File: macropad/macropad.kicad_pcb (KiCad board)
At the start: 2 copper layers, 19.9 x 58.5 mm, 4 parts, among them SW1 SW_Push, SW2 SW_Push, SW3 SW_Push, U1 MOUDLE-SEEEDUINO-XIAO

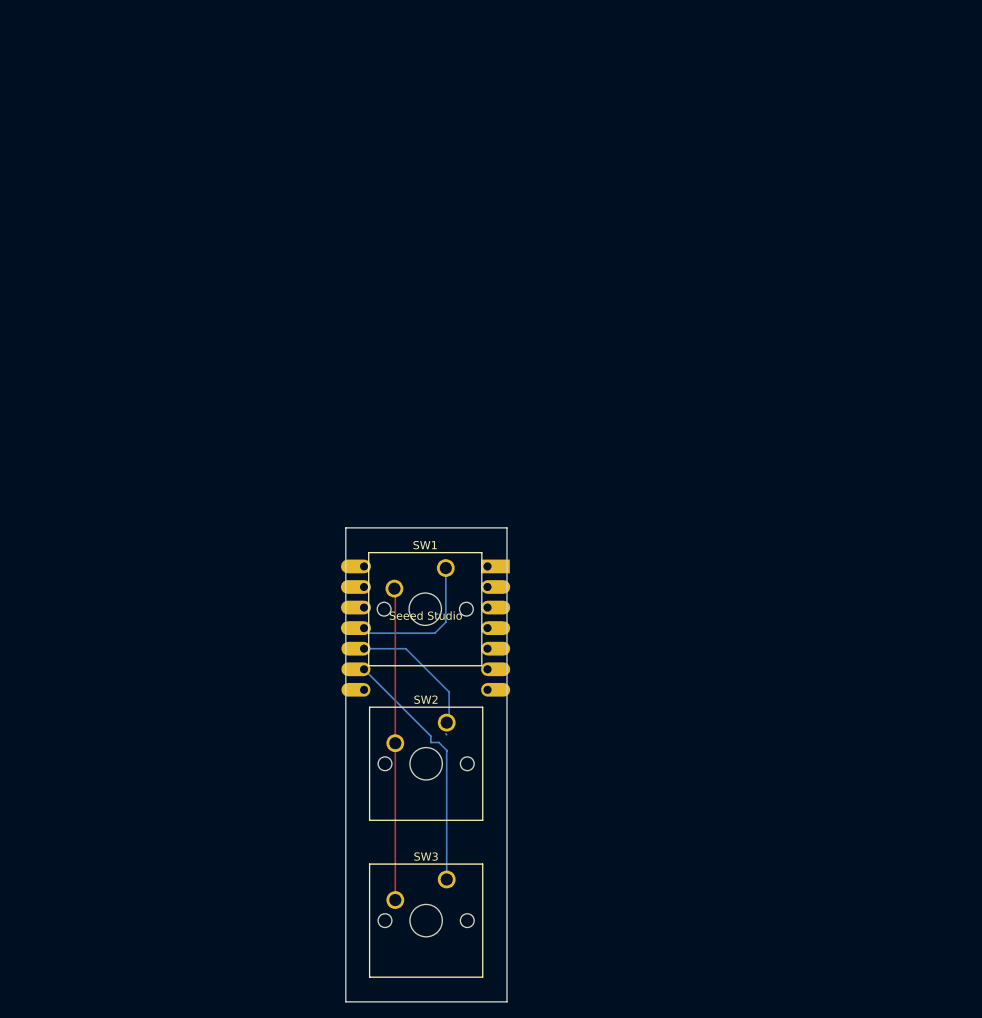
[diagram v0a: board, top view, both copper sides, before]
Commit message: Footprint edits
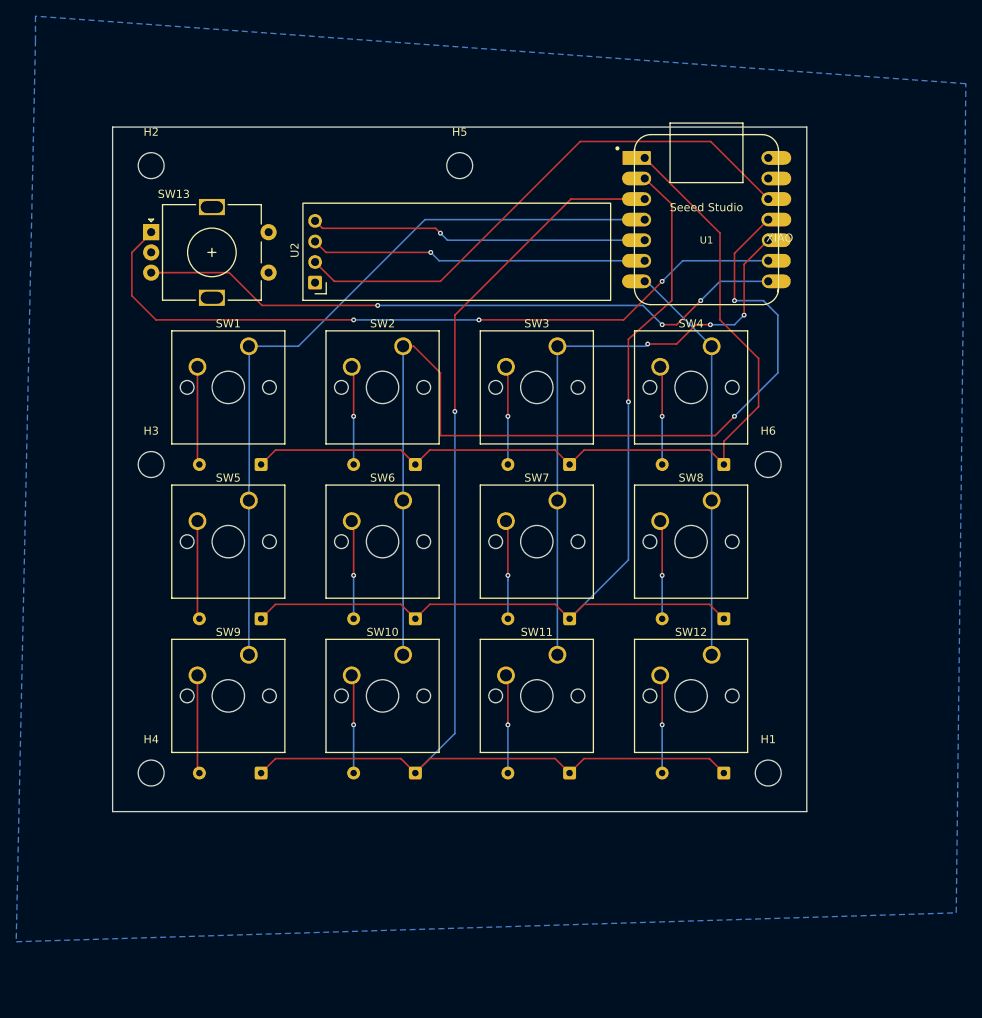
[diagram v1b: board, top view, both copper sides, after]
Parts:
- added D1: 1N4148, Diode_THT:D_DO-35_SOD27_P7.62mm_Horizontal, B.Cu at (94.5, 66.7)
- added D10: 1N4148, Diode_THT:D_DO-35_SOD27_P7.62mm_Horizontal, B.Cu at (113.6, 104.8)
- added D11: 1N4148, Diode_THT:D_DO-35_SOD27_P7.62mm_Horizontal, B.Cu at (132.6, 104.8)
- added D12: 1N4148, Diode_THT:D_DO-35_SOD27_P7.62mm_Horizontal, B.Cu at (151.7, 104.8)
- added D2: 1N4148, Diode_THT:D_DO-35_SOD27_P7.62mm_Horizontal, B.Cu at (113.6, 66.7)
- added D3: 1N4148, Diode_THT:D_DO-35_SOD27_P7.62mm_Horizontal, B.Cu at (132.6, 66.7)
- added D4: 1N4148, Diode_THT:D_DO-35_SOD27_P7.62mm_Horizontal, B.Cu at (151.7, 66.7)
- added D5: 1N4148, Diode_THT:D_DO-35_SOD27_P7.62mm_Horizontal, B.Cu at (94.5, 85.7)
- added D6: 1N4148, Diode_THT:D_DO-35_SOD27_P7.62mm_Horizontal, B.Cu at (113.6, 85.7)
- added D7: 1N4148, Diode_THT:D_DO-35_SOD27_P7.62mm_Horizontal, B.Cu at (132.6, 85.7)
- added D8: 1N4148, Diode_THT:D_DO-35_SOD27_P7.62mm_Horizontal, B.Cu at (151.7, 85.7)
- added D9: 1N4148, Diode_THT:D_DO-35_SOD27_P7.62mm_Horizontal, B.Cu at (94.5, 104.8)
- added H1: MountingHole, MountingHole:MountingHole_3.2mm_M3, F.Cu at (157.2, 104.8)
- added H2: MountingHole, MountingHole:MountingHole_3.2mm_M3, F.Cu at (81.0, 29.8)
- added H3: MountingHole, MountingHole:MountingHole_3.2mm_M3, F.Cu at (81.0, 66.7)
- added H4: MountingHole, MountingHole:MountingHole_3.2mm_M3, F.Cu at (81.0, 104.8)
- added H5: MountingHole, MountingHole:MountingHole_3.2mm_M3, F.Cu at (119.1, 29.8)
- added H6: MountingHole, MountingHole:MountingHole_3.2mm_M3, F.Cu at (157.2, 66.7)
- added SW10: SW_Push, Button_Switch_Keyboard:SW_Cherry_MX_1.00u_PCB, F.Cu at (112.1, 90.2)
- added SW11: SW_Push, Button_Switch_Keyboard:SW_Cherry_MX_1.00u_PCB, F.Cu at (131.1, 90.2)
- added SW12: SW_Push, Button_Switch_Keyboard:SW_Cherry_MX_1.00u_PCB, F.Cu at (150.2, 90.2)
- added SW13: RotaryEncoder_Switch, Rotary_Encoder:RotaryEncoder_Alps_EC11E-Switch_Vertical_H20mm, F.Cu at (81.0, 38.0)
- added SW4: SW_Push, Button_Switch_Keyboard:SW_Cherry_MX_1.00u_PCB, F.Cu at (150.2, 52.1)
- added SW5: SW_Push, Button_Switch_Keyboard:SW_Cherry_MX_1.00u_PCB, F.Cu at (93.0, 71.1)
- added SW6: SW_Push, Button_Switch_Keyboard:SW_Cherry_MX_1.00u_PCB, F.Cu at (112.1, 71.1)
- added SW7: SW_Push, Button_Switch_Keyboard:SW_Cherry_MX_1.00u_PCB, F.Cu at (131.1, 71.1)
- added SW8: SW_Push, Button_Switch_Keyboard:SW_Cherry_MX_1.00u_PCB, F.Cu at (150.2, 71.1)
- added SW9: SW_Push, Button_Switch_Keyboard:SW_Cherry_MX_1.00u_PCB, F.Cu at (93.0, 90.2)
- added U2: ER_OLEDM0.91_1x-I2C, Display:ER_OLEDM0.91_1x-I2C, F.Cu at (101.2, 44.2)
- U1: moved to F.Cu
- moved SW3 67.3 mm to (131.1, 52.1)
- moved U1 61.2 mm to (149.5, 36.4), turned to 0 degrees
- moved SW2 46.8 mm to (112.1, 52.1)
- moved SW1 36.6 mm to (93.0, 52.1)
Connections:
- SW1 pad 1: Net-(U1-PA6_A10_D10_MOSI) -> Col 0
- SW1 pad 2: GND -> Net-(D1-A)
- SW2 pad 1: Net-(U1-PA5_A9_D9_MISO) -> Col 1
- SW2 pad 2: GND -> Net-(D2-A)
- SW3 pad 1: Net-(U1-PA7_A8_D8_SCK) -> Col 2
- SW3 pad 2: GND -> Net-(D3-A)
- U1 pad 1: unconnected-(U1-PA02_A0_D0-Pad1) -> Row 0
- U1 pad 10: Net-(U1-PA5_A9_D9_MISO) -> Col 2
- U1 pad 11: Net-(U1-PA6_A10_D10_MOSI) -> Col 1
- U1 pad 12: unconnected-(U1-3V3-Pad12) -> VCC
- U1 pad 2: unconnected-(U1-PA4_A1_D1-Pad2) -> Row 1
- U1 pad 3: unconnected-(U1-PA10_A2_D2-Pad3) -> Row 2
- U1 pad 4: unconnected-(U1-PA11_A3_D3-Pad4) -> Col 0
- U1 pad 5: unconnected-(U1-PA8_A4_D4_SDA-Pad5) -> Net-(U1-PA8_A4_D4_SDA)
- U1 pad 6: unconnected-(U1-PA9_A5_D5_SCL-Pad6) -> Net-(U1-PA9_A5_D5_SCL)
- U1 pad 7: unconnected-(U1-PB08_A6_D6_TX-Pad7) -> Col 3
- U1 pad 8: unconnected-(U1-PB09_A7_D7_RX-Pad8) -> Net-(U1-PB09_A7_D7_RX)
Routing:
- net Row 2: track 0.00 -> 149.5 mm, vias 0 -> 1
- net Row 1: track 0.00 -> 122.8 mm, vias 0 -> 1
- net Col 1: track 0.00 -> 121.7 mm, vias 0 -> 2
- net Row 0: track 0.00 -> 107.1 mm
- net Col 0: track 0.00 -> 94.1 mm
- net Net-(U1-PB09_A7_D7_RX): track 0.00 -> 81.1 mm, vias 0 -> 3
- net Col 2: track 0.00 -> 73.2 mm, vias 0 -> 3
- net VCC: track 0.00 -> 67.0 mm
- net Net-(U1-PA7_A8_D8_SCK): track 31.0 -> 91.7 mm, vias 0 -> 3
- net Col 3: track 0.00 -> 49.7 mm
- net Net-(U1-PA9_A5_D5_SCL): track 0.00 -> 41.7 mm, vias 0 -> 1
- net Net-(U1-PA8_A4_D4_SDA): track 0.00 -> 41.7 mm, vias 0 -> 1
- net GND: track 37.8 -> 0.00 mm
- net Net-(U1-PA6_A10_D10_MOSI): track 17.6 -> 0.00 mm
- net Net-(U1-PA5_A9_D9_MISO): track 16.5 -> 0.00 mm
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- added copper zone on B.Cu, net GND
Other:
- board size 19.9 x 58.5 mm -> 85.7 x 84.5 mm

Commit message: Add rotary encoder step file
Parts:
- SW1, SW10, SW11, SW12, SW2, SW3, SW4, SW5, SW6, SW7, SW8, SW9: footprint Button_Switch_Keyboard:SW_Cherry_MX_1.00u_PCB -> footprints:SW_Cherry_MX_1.00u_PCB_(3D_STEP)
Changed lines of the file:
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@@
 		(embedded_fonts no)
 	)
-	(footprint "Button_Switch_Keyboard:SW_Cherry_MX_1.00u_PCB"
+	(footprint "footprints:SW_Cherry_MX_1.00u_PCB_(3D_STEP)"
 		(layer "F.Cu")
 		(at 112.0775 71.12)
@@
 		(embedded_fonts no)
 		(model "${KICAD10_3DMODEL_DIR}/Button_Switch_Keyboard.3dshapes/SW_Cherry_MX_1.00u_PCB.step"
+			(hide yes)
 			(offset
 				(xyz 0 0 0)
@@
 			)
 		)
+		(model "${KIPRJMOD}/kicad_care_package/MX .STEP"
+			(offset
+				(xyz 4.75 2.25 5.75)
+			)
+			(scale
+				(xyz 1 1 1)
+			)
+			(rotate
+				(xyz -90 -0 -180)
+			)
+		)
 	)
-	(footprint "Button_Switch_Keyboard:SW_Cherry_MX_1.00u_PCB"
+	(footprint "footprints:SW_Cherry_MX_1.00u_PCB_(3D_STEP)"
 		(layer "F.Cu")
 		(at 112.0775 52.07)
@@
 		(embedded_fonts no)
 		(model "${KICAD10_3DMODEL_DIR}/Button_Switch_Keyboard.3dshapes/SW_Cherry_MX_1.00u_PCB.step"
+			(hide yes)
 			(offset
 				(xyz 0 0 0)
@@
 			)
 		)
+		(model "${KIPRJMOD}/kicad_care_package/MX .STEP"
+			(offset
+				(xyz 4.75 2.25 5.75)
+			)
+			(scale
+				(xyz 1 1 1)
+			)
+			(rotate
+				(xyz -90 -0 -180)
+			)
+		)
 	)
 	(footprint "MountingHole:MountingHole_3.2mm_M3"
@@
 		(embedded_fonts no)
 	)
-	(footprint "Button_Switch_Keyboard:SW_Cherry_MX_1.00u_PCB"
+	(footprint "footprints:SW_Cherry_MX_1.00u_PCB_(3D_STEP)"
 		(layer "F.Cu")
 		(at 150.1775 90.17)
@@
 		(embedded_fonts no)
 		(model "${KICAD10_3DMODEL_DIR}/Button_Switch_Keyboard.3dshapes/SW_Cherry_MX_1.00u_PCB.step"
+			(hide yes)
 			(offset
 				(xyz 0 0 0)
@@
 			)
 		)
+		(model "${KIPRJMOD}/kicad_care_package/MX .STEP"
+			(offset
+				(xyz 4.75 2.25 5.75)
+			)
+			(scale
+				(xyz 1 1 1)
+			)
+			(rotate
+				(xyz -90 -0 -180)
+			)
+		)
 	)
-	(footprint "Button_Switch_Keyboard:SW_Cherry_MX_1.00u_PCB"
+	(footprint "footprints:SW_Cherry_MX_1.00u_PCB_(3D_STEP)"
 		(layer "F.Cu")
 		(at 93.0275 52.07)
@@
 		(embedded_fonts no)
 		(model "${KICAD10_3DMODEL_DIR}/Button_Switch_Keyboard.3dshapes/SW_Cherry_MX_1.00u_PCB.step"
+			(hide yes)
 			(offset
 				(xyz 0 0 0)
@@
 			)
 		)
+		(model "${KIPRJMOD}/kicad_care_package/MX .STEP"
+			(offset
+				(xyz 4.75 2.25 5.75)
+			)
+			(scale
+				(xyz 1 1 1)
+			)
+			(rotate
+				(xyz -90 -0 -180)
+			)
+		)
 	)
-	(footprint "Button_Switch_Keyboard:SW_Cherry_MX_1.00u_PCB"
+	(footprint "footprints:SW_Cherry_MX_1.00u_PCB_(3D_STEP)"
 		(layer "F.Cu")
 		(at 93.0275 90.17)
@@
 		(embedded_fonts no)
 		(model "${KICAD10_3DMODEL_DIR}/Button_Switch_Keyboard.3dshapes/SW_Cherry_MX_1.00u_PCB.step"
+			(hide yes)
 			(offset
 				(xyz 0 0 0)
@@
 			)
 		)
+		(model "${KIPRJMOD}/kicad_care_package/MX .STEP"
+			(offset
+				(xyz 4.75 2.25 5.75)
+			)
+			(scale
+				(xyz 1 1 1)
+			)
+			(rotate
+				(xyz -90 -0 -180)
+			)
+		)
 	)
 	(footprint "MountingHole:MountingHole_3.2mm_M3"
@@
 		(embedded_fonts no)
 	)
-	(footprint "Button_Switch_Keyboard:SW_Cherry_MX_1.00u_PCB"
+	(footprint "footprints:SW_Cherry_MX_1.00u_PCB_(3D_STEP)"
 		(layer "F.Cu")
 		(at 112.0775 90.17)
@@
 		(embedded_fonts no)
 		(model "${KICAD10_3DMODEL_DIR}/Button_Switch_Keyboard.3dshapes/SW_Cherry_MX_1.00u_PCB.step"
+			(hide yes)
 			(offset
 				(xyz 0 0 0)
@@
 			)
 		)
+		(model "${KIPRJMOD}/kicad_care_package/MX .STEP"
+			(offset
+				(xyz 4.75 2.25 5.75)
+			)
+			(scale
+				(xyz 1 1 1)
+			)
+			(rotate
+				(xyz -90 -0 -180)
+			)
+		)
 	)
-	(footprint "Button_Switch_Keyboard:SW_Cherry_MX_1.00u_PCB"
+	(footprint "footprints:SW_Cherry_MX_1.00u_PCB_(3D_STEP)"
 		(layer "F.Cu")
 		(at 93.0275 71.12)
@@
 		(embedded_fonts no)
 		(model "${KICAD10_3DMODEL_DIR}/Button_Switch_Keyboard.3dshapes/SW_Cherry_MX_1.00u_PCB.step"
+			(hide yes)
 			(offset
 				(xyz 0 0 0)
@@
 			)
 		)
+		(model "${KIPRJMOD}/kicad_care_package/MX .STEP"
+			(offset
+				(xyz 4.75 2.25 5.75)
+			)
+			(scale
+				(xyz 1 1 1)
+			)
+			(rotate
+				(xyz -90 -0 -180)
+			)
+		)
 	)
 	(footprint "MountingHole:MountingHole_3.2mm_M3"
@@
 		)
 	)
-	(footprint "Button_Switch_Keyboard:SW_Cherry_MX_1.00u_PCB"
+	(footprint "footprints:SW_Cherry_MX_1.00u_PCB_(3D_STEP)"
 		(layer "F.Cu")
 		(at 150.1775 71.12)
@@
 		(embedded_fonts no)
 		(model "${KICAD10_3DMODEL_DIR}/Button_Switch_Keyboard.3dshapes/SW_Cherry_MX_1.00u_PCB.step"
+			(hide yes)
 			(offset
 				(xyz 0 0 0)
@@
 			)
 		)
+		(model "${KIPRJMOD}/kicad_care_package/MX .STEP"
+			(offset
+				(xyz 4.75 2.25 5.75)
+			)
+			(scale
+				(xyz 1 1 1)
+			)
+			(rotate
+				(xyz -90 -0 -180)
+			)
+		)
 	)
 	(footprint "MountingHole:MountingHole_3.2mm_M3"
@@
 		)
 	)
-	(footprint "Button_Switch_Keyboard:SW_Cherry_MX_1.00u_PCB"
+	(footprint "footprints:SW_Cherry_MX_1.00u_PCB_(3D_STEP)"
 		(layer "F.Cu")
 		(at 131.1275 90.17)
@@
 		(embedded_fonts no)
 		(model "${KICAD10_3DMODEL_DIR}/Button_Switch_Keyboard.3dshapes/SW_Cherry_MX_1.00u_PCB.step"
+			(hide yes)
 			(offset
 				(xyz 0 0 0)
@@
 			)
 		)
+		(model "${KIPRJMOD}/kicad_care_package/MX .STEP"
+			(offset
+				(xyz 4.75 2.25 5.75)
+			)
+			(scale
+				(xyz 1 1 1)
+			)
+			(rotate
+				(xyz -90 -0 -180)
+			)
+		)
 	)
-	(footprint "Button_Switch_Keyboard:SW_Cherry_MX_1.00u_PCB"
+	(footprint "footprints:SW_Cherry_MX_1.00u_PCB_(3D_STEP)"
 		(layer "F.Cu")
 		(at 131.1275 52.07)
@@
 		(embedded_fonts no)
 		(model "${KICAD10_3DMODEL_DIR}/Button_Switch_Keyboard.3dshapes/SW_Cherry_MX_1.00u_PCB.step"
+			(hide yes)
 			(offset
 				(xyz 0 0 0)
@@
 			)
 		)
+		(model "${KIPRJMOD}/kicad_care_package/MX .STEP"
+			(offset
+				(xyz 4.75 2.25 5.75)
+			)
+			(scale
+				(xyz 1 1 1)
+			)
+			(rotate
+				(xyz -90 -0 -180)
+			)
+		)
 	)
 	(footprint "MountingHole:MountingHole_3.2mm_M3"
@@
 		(embedded_fonts no)
 	)
-	(footprint "Button_Switch_Keyboard:SW_Cherry_MX_1.00u_PCB"
+	(footprint "footprints:SW_Cherry_MX_1.00u_PCB_(3D_STEP)"
 		(layer "F.Cu")
 		(at 150.1775 52.07)
@@
 		(embedded_fonts no)
 		(model "${KICAD10_3DMODEL_DIR}/Button_Switch_Keyboard.3dshapes/SW_Cherry_MX_1.00u_PCB.step"
+			(hide yes)
 			(offset
 				(xyz 0 0 0)
@@
 			)
 		)
+		(model "${KIPRJMOD}/kicad_care_package/MX .STEP"
+			(offset
+				(xyz 4.75 2.25 5.75)
+			)
+			(scale
+				(xyz 1 1 1)
+			)
+			(rotate
+				(xyz -90 -0 -180)
+			)
+		)
 	)
-	(footprint "Button_Switch_Keyboard:SW_Cherry_MX_1.00u_PCB"
+	(footprint "footprints:SW_Cherry_MX_1.00u_PCB_(3D_STEP)"
 		(layer "F.Cu")
 		(at 131.1275 71.12)
@@
 		(embedded_fonts no)
 		(model "${KICAD10_3DMODEL_DIR}/Button_Switch_Keyboard.3dshapes/SW_Cherry_MX_1.00u_PCB.step"
+			(hide yes)
 			(offset
 				(xyz 0 0 0)
@@
 			)
 		)
+		(model "${KIPRJMOD}/kicad_care_package/MX .STEP"
+			(offset
+				(xyz 4.75 2.25 5.75)
+			)
+			(scale
+				(xyz 1 1 1)
+			)
+			(rotate
+				(xyz -90 -0 -180)
+			)
+		)

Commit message: Add Xiao and OLED STEP file
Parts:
- U2: footprint Display:ER_OLEDM0.91_1x-I2C -> footprints:ER_OLEDM0.91_1x-I2C_(3D_STEP)
